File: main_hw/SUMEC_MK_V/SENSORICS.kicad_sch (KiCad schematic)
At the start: 16 parts, among them J10 Conn_01x03_Pin, J11 Conn_01x03_Pin, J12 Conn_01x03_Pin, J13 Conn_01x03_Pin, J5 Conn_01x04_Pin, J6 Conn_01x06_Pin, J7 Conn_01x03_Pin, J8 Conn_01x03_Pin, J9 Conn_01x03_Pin, U6 BMI088

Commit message: 67yfhtgftu
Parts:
- renumbered R28 to R29, R29 to R30
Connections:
- net SHARP_L: now also J13.1 (Pin_1); no longer J12.1 (Pin_1)
- net SHARP_R: now also J12.1 (Pin_1); no longer J13.1 (Pin_1)

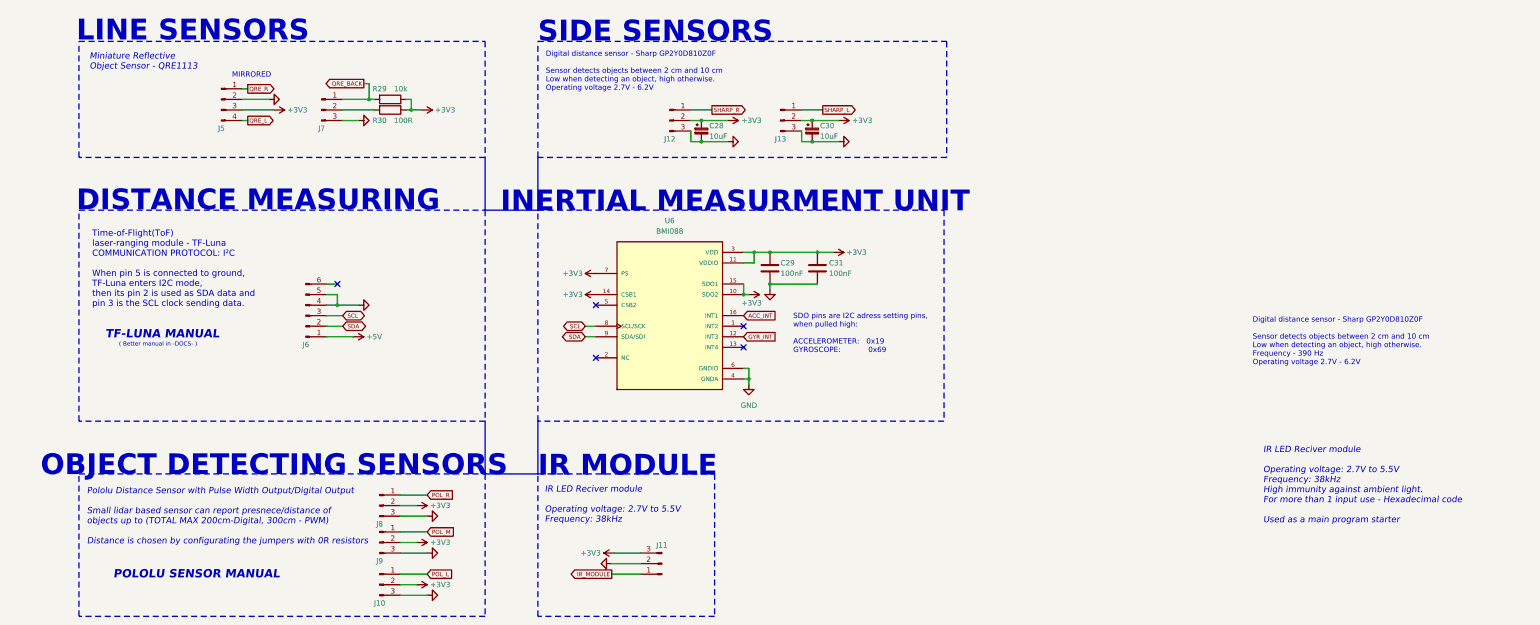
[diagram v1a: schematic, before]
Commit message: MK5 bugfix fixed POL_L, minor changes, deleted nSLEEP and nFault connections to the MCU
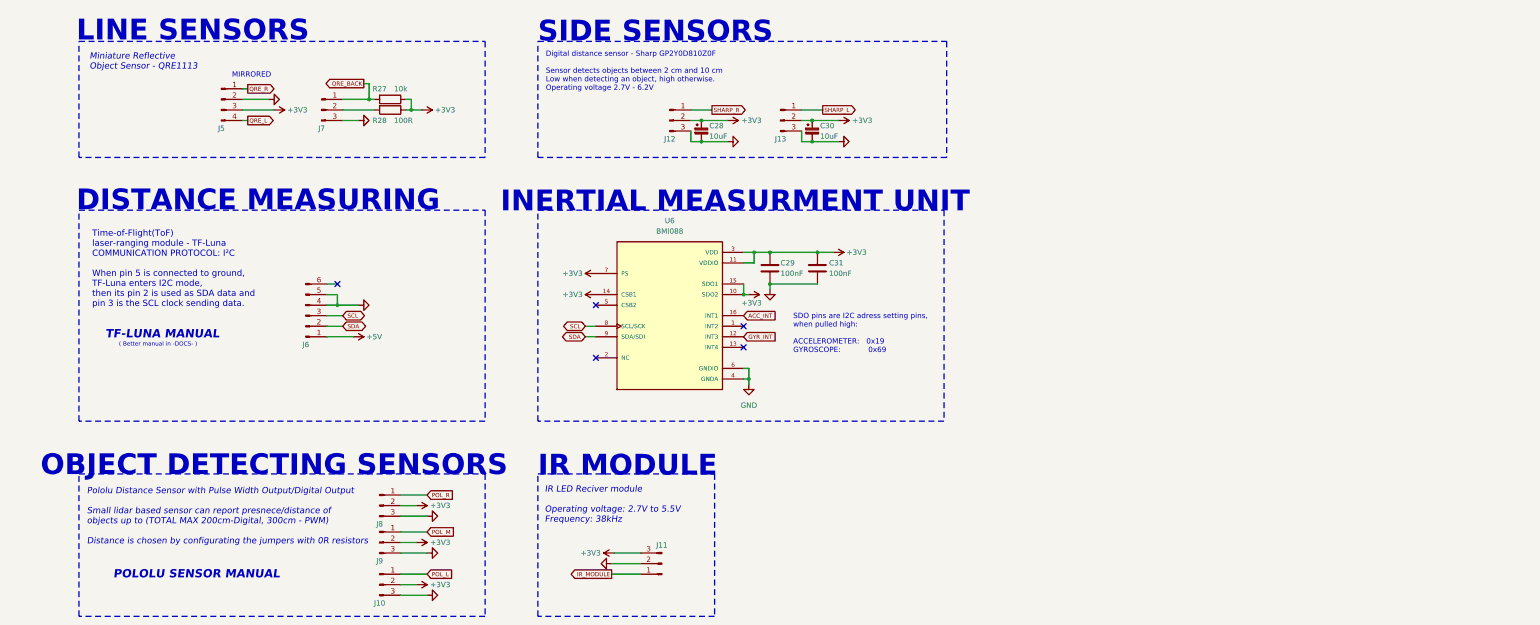
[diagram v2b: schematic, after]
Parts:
- renumbered R29 to R27, R30 to R28
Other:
- note removed: "Digital distance sensor - Sharp GP2Y0D810Z0F Sensor detects objects between 2 cm and 10 cm Low when detecting an object, high otherwise. Frequency - 390 Hz Operating voltage 2.7V - 6.2V"
- note removed: "IR LED Reciver module Operating voltage: 2.7V to 5.5V Frequency: 38kHz High immunity against ambient light. For more than 1 input use - Hexadecimal code Used as a main program starter"

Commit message: updates to mk5
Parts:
- renumbered C28 to C27, C29 to C28, C30 to C29, C31 to C30
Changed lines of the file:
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@@
 		(on_board yes)
 		(dnp no)
-		(property "Reference" "#PWR085"
+		(property "Reference" "#PWR083"
 			(at 81.28 104.14 0)
 			(effects
@@
 			(project "SUMEC_MK_V"
 				(path "/900bd7ac-cdf9-4a2f-8b1f-2c21e3760046/95cf1f13-726f-4490-ab38-a981f99dbdb3"
-					(reference "#PWR085")
+					(reference "#PWR083")
 					(unit 1)
 				)
@@
 		(on_board yes)
 		(dnp no)
-		(property "Reference" "#PWR096"
+		(property "Reference" "#PWR094"
 			(at 147.32 93.98 0)
 			(effects
@@
 			(project "SUMEC_MK_V"
 				(path "/900bd7ac-cdf9-4a2f-8b1f-2c21e3760046/95cf1f13-726f-4490-ab38-a981f99dbdb3"
-					(reference "#PWR096")
+					(reference "#PWR094")
 					(unit 1)
 				)
@@
 		(on_board yes)
 		(dnp no)
-		(property "Reference" "#PWR092"
+		(property "Reference" "#PWR090"
 			(at 109.22 147.32 0)
 			(effects
@@
 			(project "SUMEC_MK_V"
 				(path "/900bd7ac-cdf9-4a2f-8b1f-2c21e3760046/95cf1f13-726f-4490-ab38-a981f99dbdb3"
-					(reference "#PWR092")
+					(reference "#PWR090")
 					(unit 1)
 				)
@@
 		(on_board yes)
 		(dnp no)
-		(property "Reference" "#PWR089"
+		(property "Reference" "#PWR087"
 			(at 96.52 153.67 0)
 			(effects
@@
 			(project "SUMEC_MK_V"
 				(path "/900bd7ac-cdf9-4a2f-8b1f-2c21e3760046/95cf1f13-726f-4490-ab38-a981f99dbdb3"
-					(reference "#PWR089")
+					(reference "#PWR087")
 					(unit 1)
 				)
@@
 		(on_board yes)
 		(dnp no)
-		(property "Reference" "#PWR0106"
+		(property "Reference" "#PWR0104"
 			(at 208.28 57.15 0)
 			(effects
@@
 			(project "SUMEC_MK_V"
 				(path "/900bd7ac-cdf9-4a2f-8b1f-2c21e3760046/95cf1f13-726f-4490-ab38-a981f99dbdb3"
-					(reference "#PWR0106")
+					(reference "#PWR0104")
 					(unit 1)
 				)
@@
 		(on_board yes)
 		(dnp no)
-		(property "Reference" "C31"
+		(property "Reference" "C30"
 			(at 199.644 86.36 0)
 			(effects
@@
 			(project "SUMEC_MK_V"
 				(path "/900bd7ac-cdf9-4a2f-8b1f-2c21e3760046/95cf1f13-726f-4490-ab38-a981f99dbdb3"
-					(reference "C31")
+					(reference "C30")
 					(unit 1)
 				)
@@
 		(on_board yes)
 		(dnp no)
-		(property "Reference" "#PWR087"
+		(property "Reference" "#PWR085"
 			(at 92.71 96.52 0)
 			(effects
@@
 			(project "SUMEC_MK_V"
 				(path "/900bd7ac-cdf9-4a2f-8b1f-2c21e3760046/95cf1f13-726f-4490-ab38-a981f99dbdb3"
-					(reference "#PWR087")
+					(reference "#PWR085")
 					(unit 1)
 				)
@@
 		(on_board yes)
 		(dnp no)
-		(property "Reference" "#PWR094"
+		(property "Reference" "#PWR092"
 			(at 109.22 166.37 0)
 			(effects
@@
 			(project "SUMEC_MK_V"
 				(path "/900bd7ac-cdf9-4a2f-8b1f-2c21e3760046/95cf1f13-726f-4490-ab38-a981f99dbdb3"
-					(reference "#PWR094")
+					(reference "#PWR092")
 					(unit 1)
 				)
@@
 		(on_board yes)
 		(dnp no)
-		(property "Reference" "#PWR093"
+		(property "Reference" "#PWR091"
 			(at 109.22 156.21 0)
 			(effects
@@
 			(project "SUMEC_MK_V"
 				(path "/900bd7ac-cdf9-4a2f-8b1f-2c21e3760046/95cf1f13-726f-4490-ab38-a981f99dbdb3"
-					(reference "#PWR093")
+					(reference "#PWR091")
 					(unit 1)
 				)
@@
 		(on_board yes)
 		(dnp no)
-		(property "Reference" "#PWR0100"
+		(property "Reference" "#PWR098"
 			(at 181.61 57.15 0)
 			(effects
@@
 			(project "SUMEC_MK_V"
 				(path "/900bd7ac-cdf9-4a2f-8b1f-2c21e3760046/95cf1f13-726f-4490-ab38-a981f99dbdb3"
-					(reference "#PWR0100")
+					(reference "#PWR098")
 					(unit 1)
 				)
@@
 		(on_board yes)
 		(dnp no)
-		(property "Reference" "#PWR098"
+		(property "Reference" "#PWR096"
 			(at 151.765 156.21 0)
 			(effects
@@
 			(project "SUMEC_MK_V"
 				(path "/900bd7ac-cdf9-4a2f-8b1f-2c21e3760046/95cf1f13-726f-4490-ab38-a981f99dbdb3"
-					(reference "#PWR098")
+					(reference "#PWR096")
 					(unit 1)
 				)
@@
 		(on_board yes)
 		(dnp no)
-		(property "Reference" "#PWR0102"
+		(property "Reference" "#PWR0100"
 			(at 180.34 121.92 0)
 			(effects
@@
 			(project "SUMEC_MK_V"
 				(path "/900bd7ac-cdf9-4a2f-8b1f-2c21e3760046/95cf1f13-726f-4490-ab38-a981f99dbdb3"
-					(reference "#PWR0102")
+					(reference "#PWR0100")
 					(unit 1)
 				)
@@
 		(on_board yes)
 		(dnp no)
-		(property "Reference" "#PWR095"
+		(property "Reference" "#PWR093"
 			(at 147.32 88.9 0)
 			(effects
@@
 			(project "SUMEC_MK_V"
 				(path "/900bd7ac-cdf9-4a2f-8b1f-2c21e3760046/95cf1f13-726f-4490-ab38-a981f99dbdb3"
-					(reference "#PWR095")
+					(reference "#PWR093")
 					(unit 1)
 				)
@@
 		(on_board yes)
 		(dnp no)
-		(property "Reference" "#PWR099"
+		(property "Reference" "#PWR097"
 			(at 171.45 52.07 0)
 			(effects
@@
 			(project "SUMEC_MK_V"
 				(path "/900bd7ac-cdf9-4a2f-8b1f-2c21e3760046/95cf1f13-726f-4490-ab38-a981f99dbdb3"
-					(reference "#PWR099")
+					(reference "#PWR097")
 					(unit 1)
 				)
@@
 		(on_board yes)
 		(dnp no)
-		(property "Reference" "C30"
+		(property "Reference" "C29"
 			(at 197.485 53.34 0)
 			(effects
@@
 			(project "SUMEC_MK_V"
 				(path "/900bd7ac-cdf9-4a2f-8b1f-2c21e3760046/95cf1f13-726f-4490-ab38-a981f99dbdb3"
-					(reference "C30")
+					(reference "C29")
 					(unit 1)
 				)
@@
 		(dnp no)
 		(fields_autoplaced yes)
-		(property "Reference" "#PWR083"
+		(property "Reference" "#PWR081"
 			(at 71.12 46.99 0)
 			(effects
@@
 			(project "SUMEC_MK_V"
 				(path "/900bd7ac-cdf9-4a2f-8b1f-2c21e3760046/95cf1f13-726f-4490-ab38-a981f99dbdb3"
-					(reference "#PWR083")
+					(reference "#PWR081")
 					(unit 1)
 				)
@@
 		(dnp no)
 		(fields_autoplaced yes)
-		(property "Reference" "#PWR086"
+		(property "Reference" "#PWR084"
 			(at 92.71 52.07 0)
 			(effects
@@
 			(project "SUMEC_MK_V"
 				(path "/900bd7ac-cdf9-4a2f-8b1f-2c21e3760046/95cf1f13-726f-4490-ab38-a981f99dbdb3"
-					(reference "#PWR086")
+					(reference "#PWR084")
 					(unit 1)
 				)
@@
 		(on_board yes)
 		(dnp no)
-		(property "Reference" "#PWR090"
+		(property "Reference" "#PWR088"
 			(at 96.52 163.83 0)
 			(effects
@@
 			(project "SUMEC_MK_V"
 				(path "/900bd7ac-cdf9-4a2f-8b1f-2c21e3760046/95cf1f13-726f-4490-ab38-a981f99dbdb3"
-					(reference "#PWR090")
+					(reference "#PWR088")
 					(unit 1)
 				)
@@
 		(on_board yes)
 		(dnp no)
-		(property "Reference" "#PWR0105"
+		(property "Reference" "#PWR0103"
 			(at 198.12 52.07 0)
 			(effects
@@
 			(project "SUMEC_MK_V"
 				(path "/900bd7ac-cdf9-4a2f-8b1f-2c21e3760046/95cf1f13-726f-4490-ab38-a981f99dbdb3"
-					(reference "#PWR0105")
+					(reference "#PWR0103")
 					(unit 1)
 				)
@@
 		(on_board yes)
 		(dnp no)
-		(property "Reference" "#PWR084"
+		(property "Reference" "#PWR082"
 			(at 62.23 49.53 0)
 			(effects
@@
 			(project "SUMEC_MK_V"
 				(path "/900bd7ac-cdf9-4a2f-8b1f-2c21e3760046/95cf1f13-726f-4490-ab38-a981f99dbdb3"
-					(reference "#PWR084")
+					(reference "#PWR082")
 					(unit 1)
 				)
@@
 		(on_board yes)
 		(dnp no)
-		(property "Reference" "C29"
+		(property "Reference" "C28"
 			(at 187.96 86.36 0)
 			(effects
@@
 			(project "SUMEC_MK_V"
 				(path "/900bd7ac-cdf9-4a2f-8b1f-2c21e3760046/95cf1f13-726f-4490-ab38-a981f99dbdb3"
-					(reference "C29")
+					(reference "C28")
 					(unit 1)
 				)
@@
 		(on_board yes)
 		(dnp no)
-		(property "Reference" "#PWR088"
+		(property "Reference" "#PWR086"
 			(at 96.52 144.78 0)
 			(effects
@@
 			(project "SUMEC_MK_V"
 				(path "/900bd7ac-cdf9-4a2f-8b1f-2c21e3760046/95cf1f13-726f-4490-ab38-a981f99dbdb3"
-					(reference "#PWR088")
+					(reference "#PWR086")
 					(unit 1)
 				)
@@
 		(dnp no)
 		(fields_autoplaced yes)
-		(property "Reference" "#PWR0103"
+		(property "Reference" "#PWR0101"
 			(at 185.42 99.06 0)
 			(effects
@@
 			(project "SUMEC_MK_V"
 				(path "/900bd7ac-cdf9-4a2f-8b1f-2c21e3760046/95cf1f13-726f-4490-ab38-a981f99dbdb3"
-					(reference "#PWR0103")
+					(reference "#PWR0101")
 					(unit 1)
 				)
@@
 		(on_board yes)
 		(dnp no)
-		(property "Reference" "C28"
+		(property "Reference" "C27"
 			(at 170.815 53.34 0)
 			(effects
@@
 			(project "SUMEC_MK_V"
 				(path "/900bd7ac-cdf9-4a2f-8b1f-2c21e3760046/95cf1f13-726f-4490-ab38-a981f99dbdb3"
-					(reference "C28")
+					(reference "C27")
 					(unit 1)
 				)
@@
 		(on_board yes)
 		(dnp no)
-		(property "Reference" "#PWR0104"
+		(property "Reference" "#PWR0102"
 			(at 196.85 83.82 0)
 			(effects
@@
 			(project "SUMEC_MK_V"
 				(path "/900bd7ac-cdf9-4a2f-8b1f-2c21e3760046/95cf1f13-726f-4490-ab38-a981f99dbdb3"
-					(reference "#PWR0104")
+					(reference "#PWR0102")
 					(unit 1)
 				)
@@
 		(dnp no)
 		(fields_autoplaced yes)
-		(property "Reference" "#PWR097"
+		(property "Reference" "#PWR095"
 			(at 140.97 158.75 0)
 			(effects
@@
 			(project "SUMEC_MK_V"
 				(path "/900bd7ac-cdf9-4a2f-8b1f-2c21e3760046/95cf1f13-726f-4490-ab38-a981f99dbdb3"
-					(reference "#PWR097")
+					(reference "#PWR095")
 					(unit 1)
 				)
@@
 		(on_board yes)
 		(dnp no)
-		(property "Reference" "#PWR091"
+		(property "Reference" "#PWR089"
 			(at 97.79 49.53 0)
 			(effects
@@
 			(project "SUMEC_MK_V"
 				(path "/900bd7ac-cdf9-4a2f-8b1f-2c21e3760046/95cf1f13-726f-4490-ab38-a981f99dbdb3"
-					(reference "#PWR091")
+					(reference "#PWR089")
 					(unit 1)
 				)
@@
 		(on_board yes)
 		(dnp no)
-		(property "Reference" "#PWR0101"
+		(property "Reference" "#PWR099"
 			(at 176.53 93.98 0)
 			(effects
@@
 			(project "SUMEC_MK_V"
 				(path "/900bd7ac-cdf9-4a2f-8b1f-2c21e3760046/95cf1f13-726f-4490-ab38-a981f99dbdb3"
-					(reference "#PWR0101")
+					(reference "#PWR099")
 					(unit 1)
 				)

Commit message: MK5 PCB rework
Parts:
- removed C27, C29: 10uF, Capacitor_Tantalum_SMD:CP_EIA-3216-18_Kemet-A_Pad1.58x1.35mm_HandSolder, symbol Device:C_Polarized_Small
- removed C28, C30: 100nF, Capacitor_SMD:C_0805_2012Metric_Pad1.18x1.45mm_HandSolder, symbol Device:C
- removed J10, J12, J13, J7, J8, J9: Conn_01x03_Pin, Connector_Molex:Molex_PicoBlade_53398-0371_1x03-1MP_P1.25mm_Vertical, symbol Connector:Conn_01x03_Pin
- removed J11: Conn_01x03_Pin, Connector_PinHeader_2.54mm:PinHeader_1x03_P2.54mm_Vertical, symbol Connector:Conn_01x03_Pin
- removed J5: Conn_01x04_Pin, Connector_Molex:Molex_PicoBlade_53398-0471_1x04-1MP_P1.25mm_Vertical, symbol Connector:Conn_01x04_Pin
- removed J6: Conn_01x06_Pin, Connector_Molex:Molex_PicoBlade_53398-0671_1x06-1MP_P1.25mm_Vertical, symbol Connector:Conn_01x06_Pin
- removed R27: 10k, Resistor_SMD:R_0805_2012Metric_Pad1.20x1.40mm_HandSolder, symbol Device:R
- removed R28: 100R, Resistor_SMD:R_0805_2012Metric_Pad1.20x1.40mm_HandSolder, symbol Device:R
- removed U6: BMI088, finca:PQFN50P450X300X100-16N, symbol finca_lib:BMI088
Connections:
- no-connect marks 5 -> 0
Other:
- note removed: "( Better manual in -DOCS- )"
- note removed: "DISTANCE MEASURING"
- note removed: "Digital distance sensor - Sharp GP2Y0D810Z0F Sensor detects objects between 2 cm and 10 cm Low when detecting an object, high otherwise. Operating voltage 2.7V - 6.2V"
- note removed: "INERTIAL MEASURMENT UNIT"
- note removed: "IR LED Reciver module Operating voltage: 2.7V to 5.5V Frequency: 38kHz"
- note removed: "IR MODULE"
- note removed: "LINE SENSORS"
- note removed: "MIRRORED"
- note removed: "Miniature Reflective Object Sensor - QRE1113"
- note removed: "OBJECT DETECTING SENSORS"
- note removed: "POLOLU SENSOR MANUAL"
- note removed: "Pololu Distance Sensor with Pulse Width Output/Digital Output Small lidar based sensor can report presnece/distance of objects up to (TOTAL MAX 200cm-Digital, 300cm - PWM) Distance is chosen by configurating the jumpers with 0R resistors"
- note removed: "SDO pins are I2C adress setting pins, when pulled high: ACCELEROMETER: 0x19 GYROSCOPE: 0x69"
- note removed: "SIDE SENSORS"
- note removed: "TF-LUNA MANUAL"
- note removed: "Time-of-Flight(ToF) laser-ranging module - TF-Luna COMMUNICATION PROTOCOL: I²C When pin 5 is connected to ground, TF-Luna enters I2C mode, then its pin 2 is used as SDA data and pin 3 is the SCL clock sending data."
